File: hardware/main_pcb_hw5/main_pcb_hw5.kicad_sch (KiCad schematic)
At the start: 27 parts, among them J1 MEGA TOP, J10 GBA_Slot, J2 MEGA BOTTOM, J3 CART SLOT TOP ROW, J4 CART SLOT BOTTOM ROW, J5 MEGA SIDE, J6 5V USB, J7 Conn_01x07, J8 EXP2, J9 EXP1, M2_1 Screw_Terminal_01x01, M2_2 Screw_Terminal_01x01, M2_3 Screw_Terminal_01x01, M2_4 Screw_Terminal_01x01, M2_5 Screw_Terminal_01x01, M2_6 Screw_Terminal_01x01, M2_7 Screw_Terminal_01x01, M2_8 Screw_Terminal_01x01, M2_9 Screw_Terminal_01x01, SW1 VOLTAGE, SW2 POWER

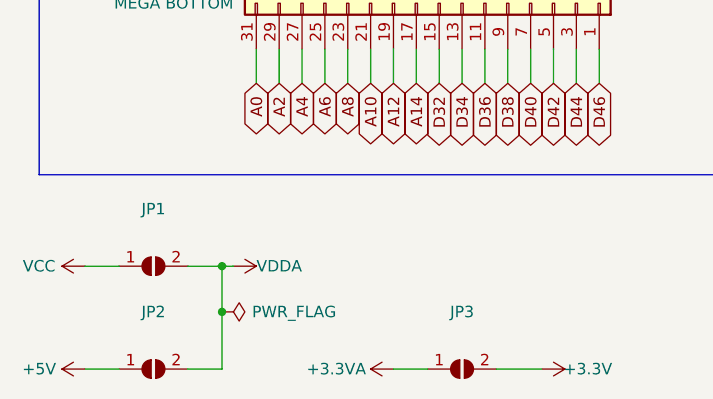
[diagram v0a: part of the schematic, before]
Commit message: relink footprints to symbols
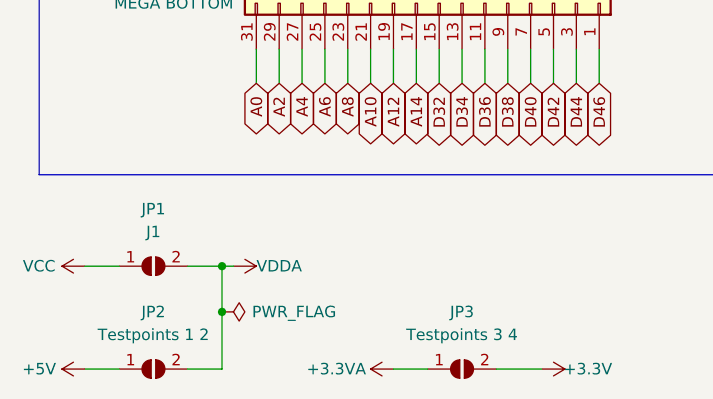
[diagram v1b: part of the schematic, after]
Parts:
- C1: footprint (none) -> Capacitor_THT:CP_Radial_D8.0mm_P3.50mm
- D1: footprint (none) -> LED_THT:LED_D3.0mm
- J10: footprint (none) -> !OSCR:GBA_Slot
- J7: footprint (none) -> Connector_PinHeader_2.54mm:PinHeader_1x07_P2.54mm_Vertical
- JP1: value (none) -> J1; footprint (none) -> Jumper:SolderJumper-2_P1.3mm_Open_Pad1.0x1.5mm
- JP2: value (none) -> Testpoints 1 2; footprint (none) -> Jumper:SolderJumper-2_P1.3mm_Open_Pad1.0x1.5mm
- JP3: value (none) -> Testpoints 3 4; footprint (none) -> Jumper:SolderJumper-2_P1.3mm_Open_Pad1.0x1.5mm
- M2_1, M2_2, M2_3, M2_4, M2_5, M2_6, M2_7, M2_8, M2_9: footprint (none) -> MountingHole:MountingHole_2.2mm_M2_ISO7380_Pad
- R1: footprint (none) -> Resistor_THT:R_Axial_DIN0207_L6.3mm_D2.5mm_P10.16mm_Horizontal
- SW1, SW2: footprint (none) -> Button_Switch_THT:SW_CuK_OS102011MA1QN1_SPDT_Angled

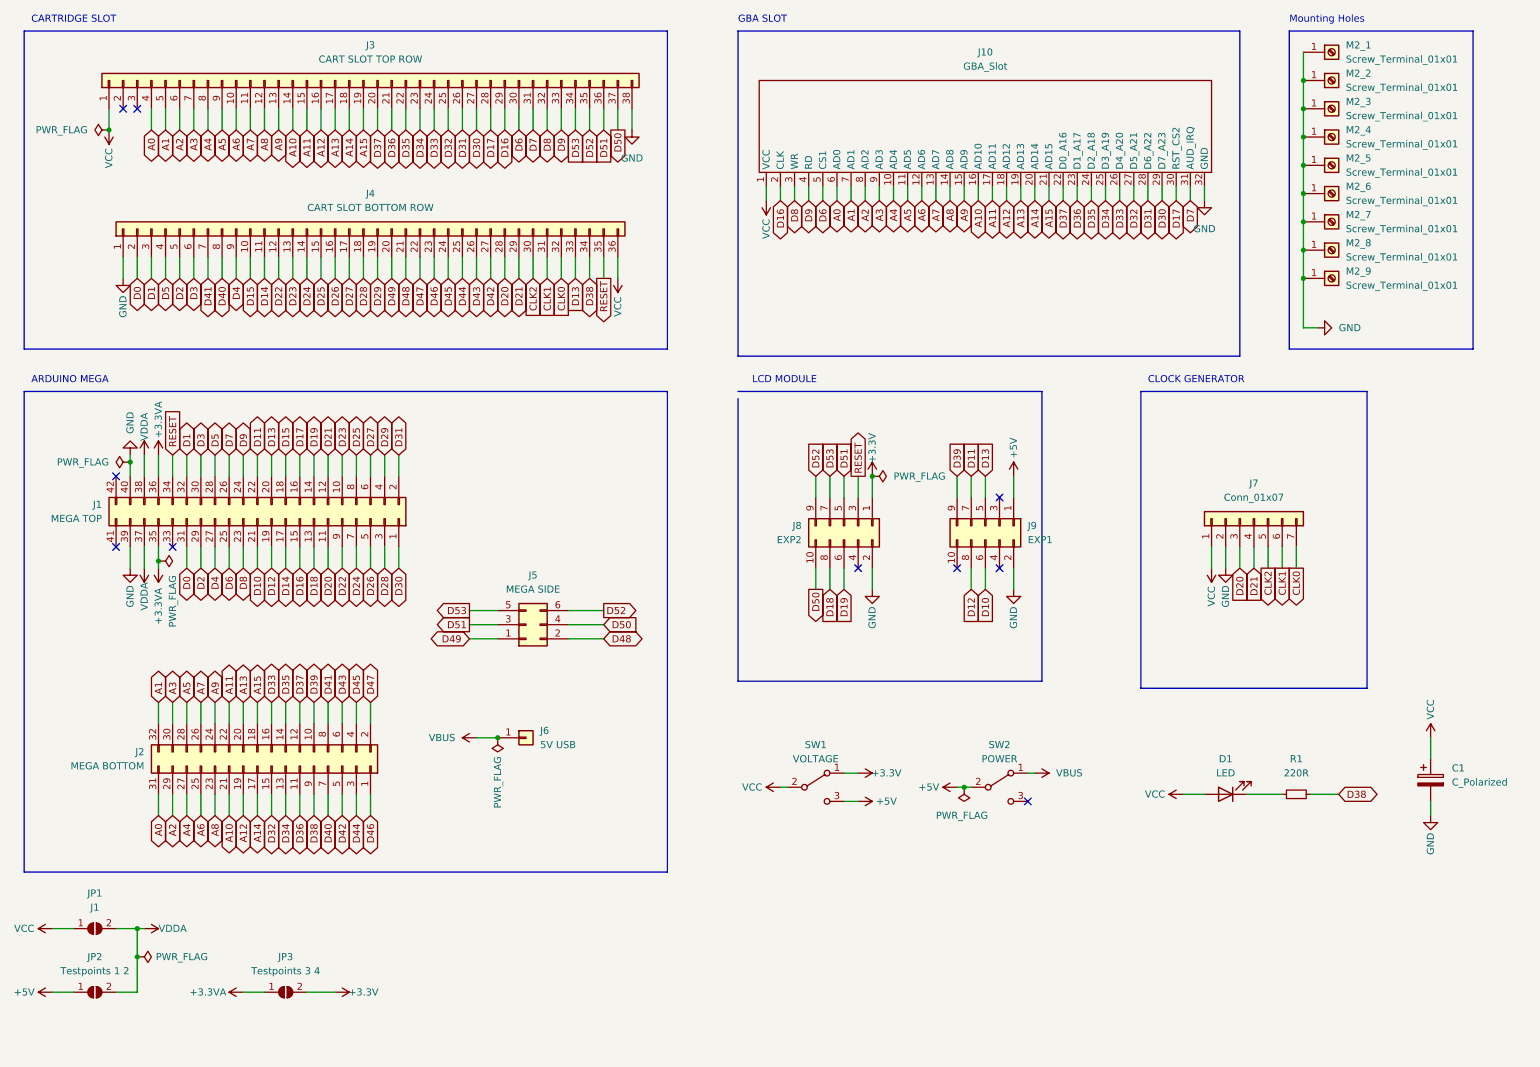
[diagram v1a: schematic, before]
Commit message: Move main PCB updates to clean branch
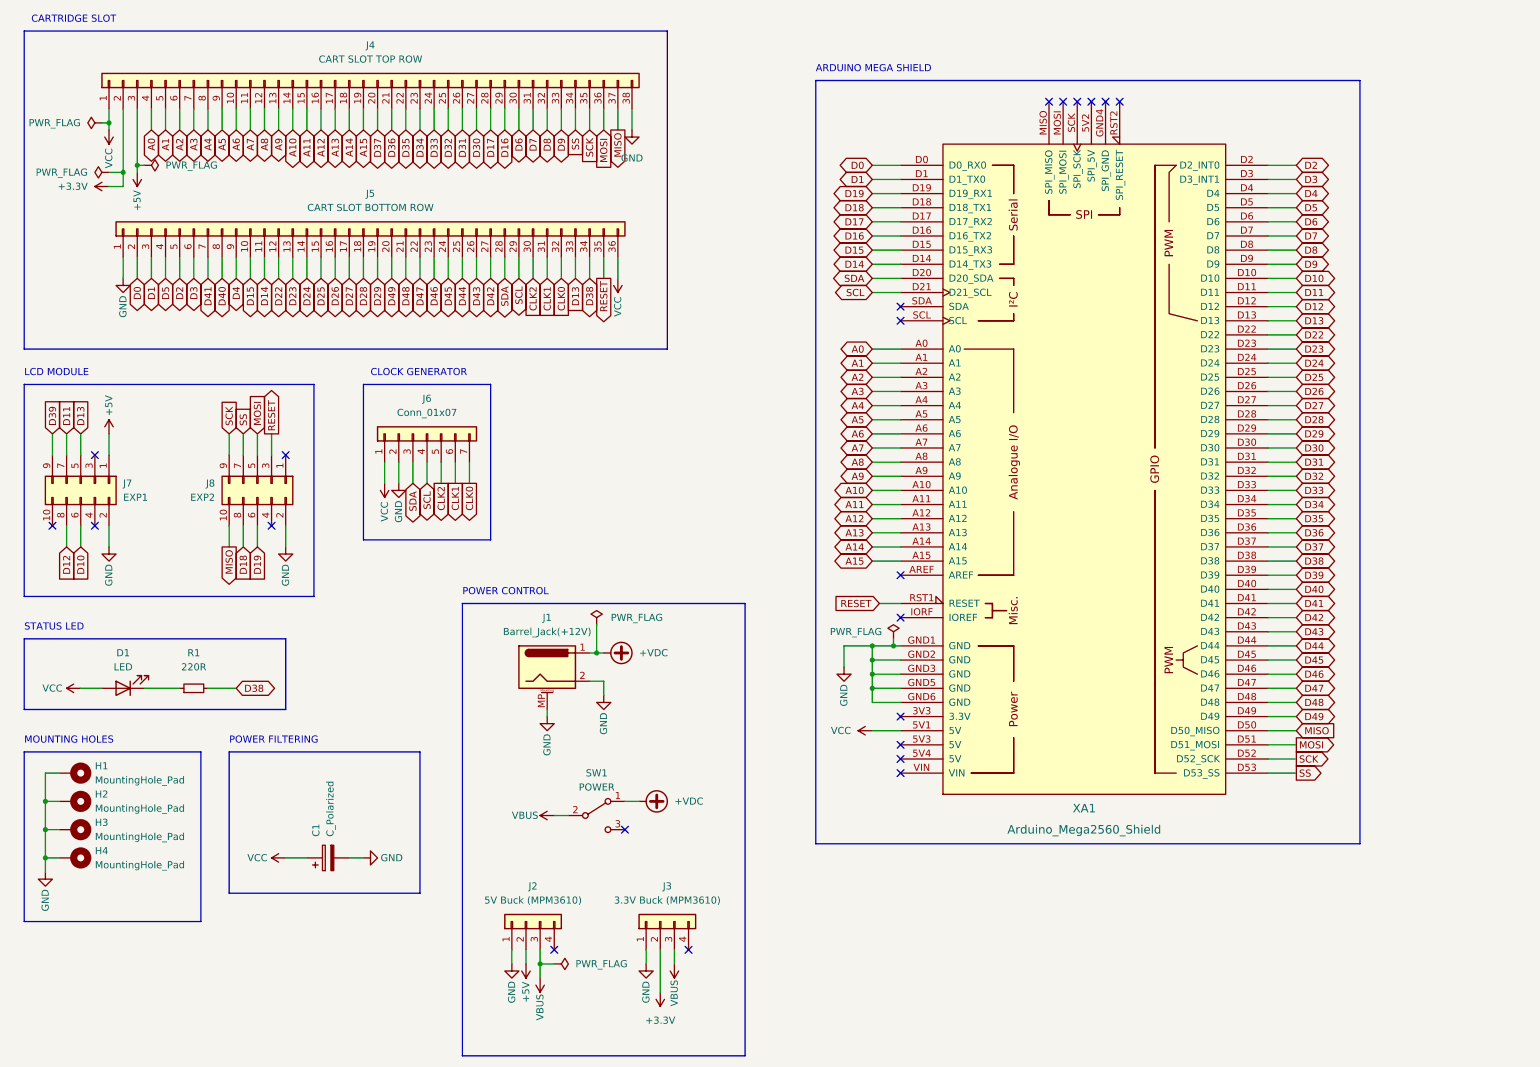
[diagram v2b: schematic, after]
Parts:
- removed J1: MEGA TOP, Connector_PinSocket_2.54mm:PinSocket_2x21_P2.54mm_Vertical, symbol Connector_Generic:Conn_02x21_Odd_Even
- removed J10: GBA_Slot, !OSCR:GBA_Slot, symbol !OSCR:GBA_Slot
- removed J2: MEGA BOTTOM, Connector_PinSocket_2.54mm:PinSocket_2x16_P2.54mm_Vertical, symbol Connector_Generic:Conn_02x16_Odd_Even
- removed J5: MEGA SIDE, Connector_PinSocket_2.54mm:PinSocket_2x03_P2.54mm_Vertical, symbol Connector_Generic:Conn_02x03_Odd_Even
- removed J6: 5V USB, Connector_PinHeader_2.54mm:PinHeader_1x01_P2.54mm_Vertical, symbol Connector_Generic:Conn_01x01
- removed JP1: J1, Jumper:SolderJumper-2_P1.3mm_Open_Pad1.0x1.5mm, symbol Jumper:SolderJumper_2_Open
- removed JP2: Testpoints 1 2, Jumper:SolderJumper-2_P1.3mm_Open_Pad1.0x1.5mm, symbol Jumper:SolderJumper_2_Open
- removed JP3: Testpoints 3 4, Jumper:SolderJumper-2_P1.3mm_Open_Pad1.0x1.5mm, symbol Jumper:SolderJumper_2_Open
- removed M2_1, M2_2, M2_3, M2_4, M2_5, M2_6, M2_7, M2_8, M2_9: Screw_Terminal_01x01, MountingHole:MountingHole_2.2mm_M2_ISO7380_Pad, symbol Connector:Screw_Terminal_01x01
- removed SW1: VOLTAGE, Button_Switch_THT:SW_CuK_OS102011MA1QN1_SPDT_Angled, symbol Switch:SW_SPDT
- added H1, H2, H3, H4: MountingHole_Pad, MountingHole:MountingHole_3.2mm_M3_Pad, symbol Mechanical:MountingHole_Pad
- added J1: Barrel_Jack(+12V), Connector_BarrelJack:BarrelJack_Horizontal, symbol Connector:Barrel_Jack_MountingPin
- added J2: 5V Buck (MPM3610), Connector_PinHeader_2.54mm:PinHeader_1x04_P2.54mm_Vertical, symbol Connector_Generic:Conn_01x04
- added J3: 3.3V Buck (MPM3610), Connector_PinHeader_2.54mm:PinHeader_1x04_P2.54mm_Vertical, symbol Connector_Generic:Conn_01x04
- added XA1: Arduino_Mega2560_Shield, Arduino_Library:Arduino_Mega2560_Shield, symbol arduino_boards_library:Arduino_Mega2560_Shield
- renumbered J3 to J4, J4 to J5, J7 to J6, J9 to J7, SW2 to SW1
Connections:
- net +5V: now also J4.3 (Pin_3), J2.2 (Pin_2); no longer SW1.2 (B)
- net A0: now also XA1.A0
- net A1: now also XA1.A1
- net A10: now also XA1.A10
- net A11: now also XA1.A11
- net A12: now also XA1.A12
- net A13: now also XA1.A13
- net A14: now also XA1.A14
- net A15: now also XA1.A15
- net A2: now also XA1.A2
- net A3: now also XA1.A3
- net A4: now also XA1.A4
- net A5: now also XA1.A5
- net A6: now also XA1.A6
- net A7: now also XA1.A7
- net A8: now also XA1.A8
- net A9: now also XA1.A9
- net D0: now also XA1.D0 (D0_RX0)
- net D1: now also XA1.D1 (D1_TX0)
- net D10: now also XA1.D10
- net D11: now also XA1.D11
- net D12: now also XA1.D12
- net D13: now also XA1.D13
- net D14: now also XA1.D14 (D14_TX3)
- net D15: now also XA1.D15 (D15_RX3)
- net D16: now also XA1.D16 (D16_TX2)
- net D17: now also XA1.D17 (D17_RX2)
- net D18: now also XA1.D18 (D18_TX1)
- net D19: now also XA1.D19 (D19_RX1)
- net D2: now also XA1.D2 (D2_INT0)
- net D22: now also XA1.D22
- net D23: now also XA1.D23
- net D24: now also XA1.D24
- net D25: now also XA1.D25
- net D26: now also XA1.D26
- net D27: now also XA1.D27
- net D28: now also XA1.D28
- net D29: now also XA1.D29
- net D3: now also XA1.D3 (D3_INT1)
- net D30: now also XA1.D30
- net D31: now also XA1.D31
- net D32: now also XA1.D32
- net D33: now also XA1.D33
- net D34: now also XA1.D34
- net D35: now also XA1.D35
- net D36: now also XA1.D36
- net D37: now also XA1.D37
- net D38: now also XA1.D38
- net D39: now also XA1.D39
- net D4: now also XA1.D4
- net D40: now also XA1.D40
- net D41: now also XA1.D41
- net D42: now also XA1.D42
- net D43: now also XA1.D43
- net D44: now also XA1.D44
- net D45: now also XA1.D45
- net D46: now also XA1.D46
- net D47: now also XA1.D47
- net D48: now also XA1.D48
- net D49: now also XA1.D49
- net D5: now also XA1.D5
- net D6: now also XA1.D6
- net D7: now also XA1.D7
- net D8: now also XA1.D8
- net D9: now also XA1.D9
- net GND: now also H1.1, H2.1, H3.1, H4.1, J1.2, J1.MP (MountPin), J2.1 (Pin_1), J3.1 (Pin_1), XA1.GND1 (GND), XA1.GND2 (GND), XA1.GND3 (GND), XA1.GND5 (GND), XA1.GND6 (GND)
- net RESET: now also XA1.RST1 (RESET)
- net VBUS: now also SW1.2 (B), J2.3 (Pin_3), J3.3 (Pin_3); no longer SW1.1 (A)
- net VCC: now also XA1.5V1 (5V)
- net +3.3V: now reaches J4.2 (Pin_2)
- net +3.3V: now also J3.2 (Pin_2)
- net +3V3: no longer names the net of J8.1 (Pin_1)
- net D20 renamed SDA
- net SDA: now also XA1.D20 (D20_SDA)
- net D21 renamed SCL
- net SCL: now also XA1.D21 (D21_SCL)
- net D50 renamed MISO
- net MISO: now also XA1.D50 (D50_MISO)
- net D51 renamed MOSI
- net MOSI: now also XA1.D51 (D51_MOSI)
- net D52 renamed SCK
- net SCK: now also XA1.D52 (D52_SCK)
- net D53 renamed SS
- net SS: now also XA1.D53 (D53_SS)
- new net +VDC: J1.1, SW1.1 (A)
- no-connect marks 10 -> 22
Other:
- note added: "ARDUINO MEGA SHIELD"
- note added: "MOUNTING HOLES"
- note added: "POWER CONTROL"
- note added: "POWER FILTERING"
- note added: "STATUS LED"
- note removed: "ARDUINO MEGA"
- note removed: "GBA SLOT"
- note removed: "Mounting Holes"
- title: OSCR HW5 -> OSCR Shield
- moved on the sheet: C1, D1, J6, J7, J8, R1, SW1
